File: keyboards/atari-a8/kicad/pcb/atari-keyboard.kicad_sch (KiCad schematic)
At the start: 26 parts, among them J101 PLAYER 1, J102 Conn_02x20_Odd_Even, J103 I2C DISPLAY, J104 Conn_02x20_Odd_Even, J105 Conn_02x20_Odd_Even, J106 Conn_02x20_Odd_Even, SW101 RESET, U101 MAX7219, U102 MAX7219

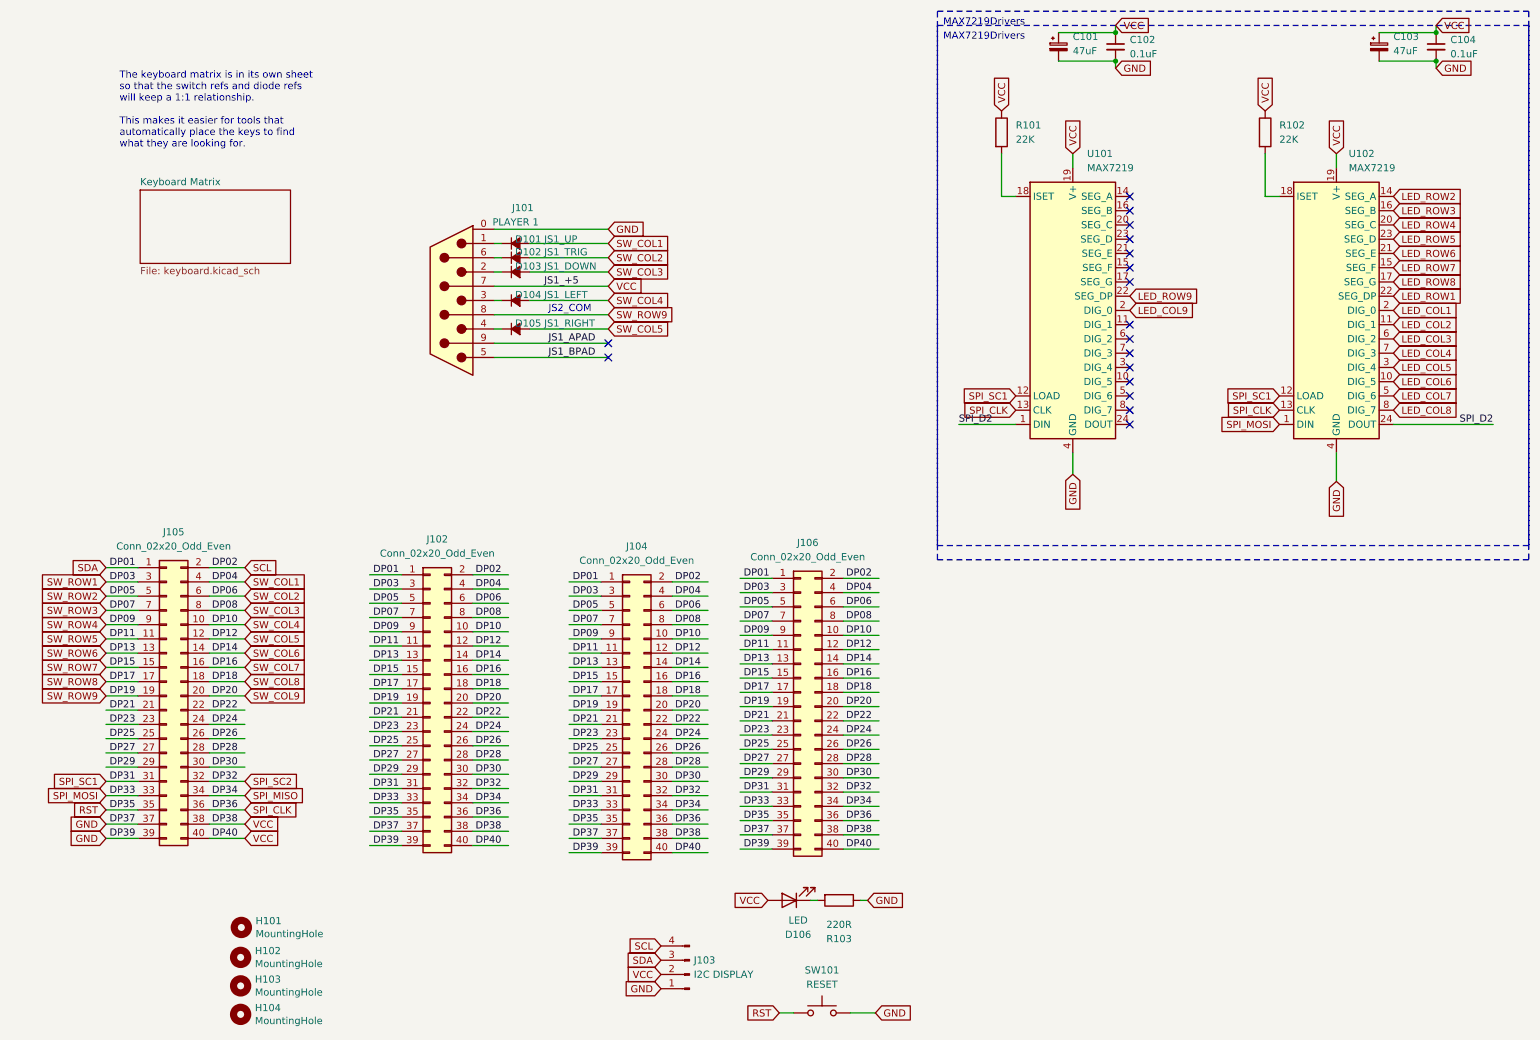
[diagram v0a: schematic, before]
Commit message: Added generating the keyboard plate
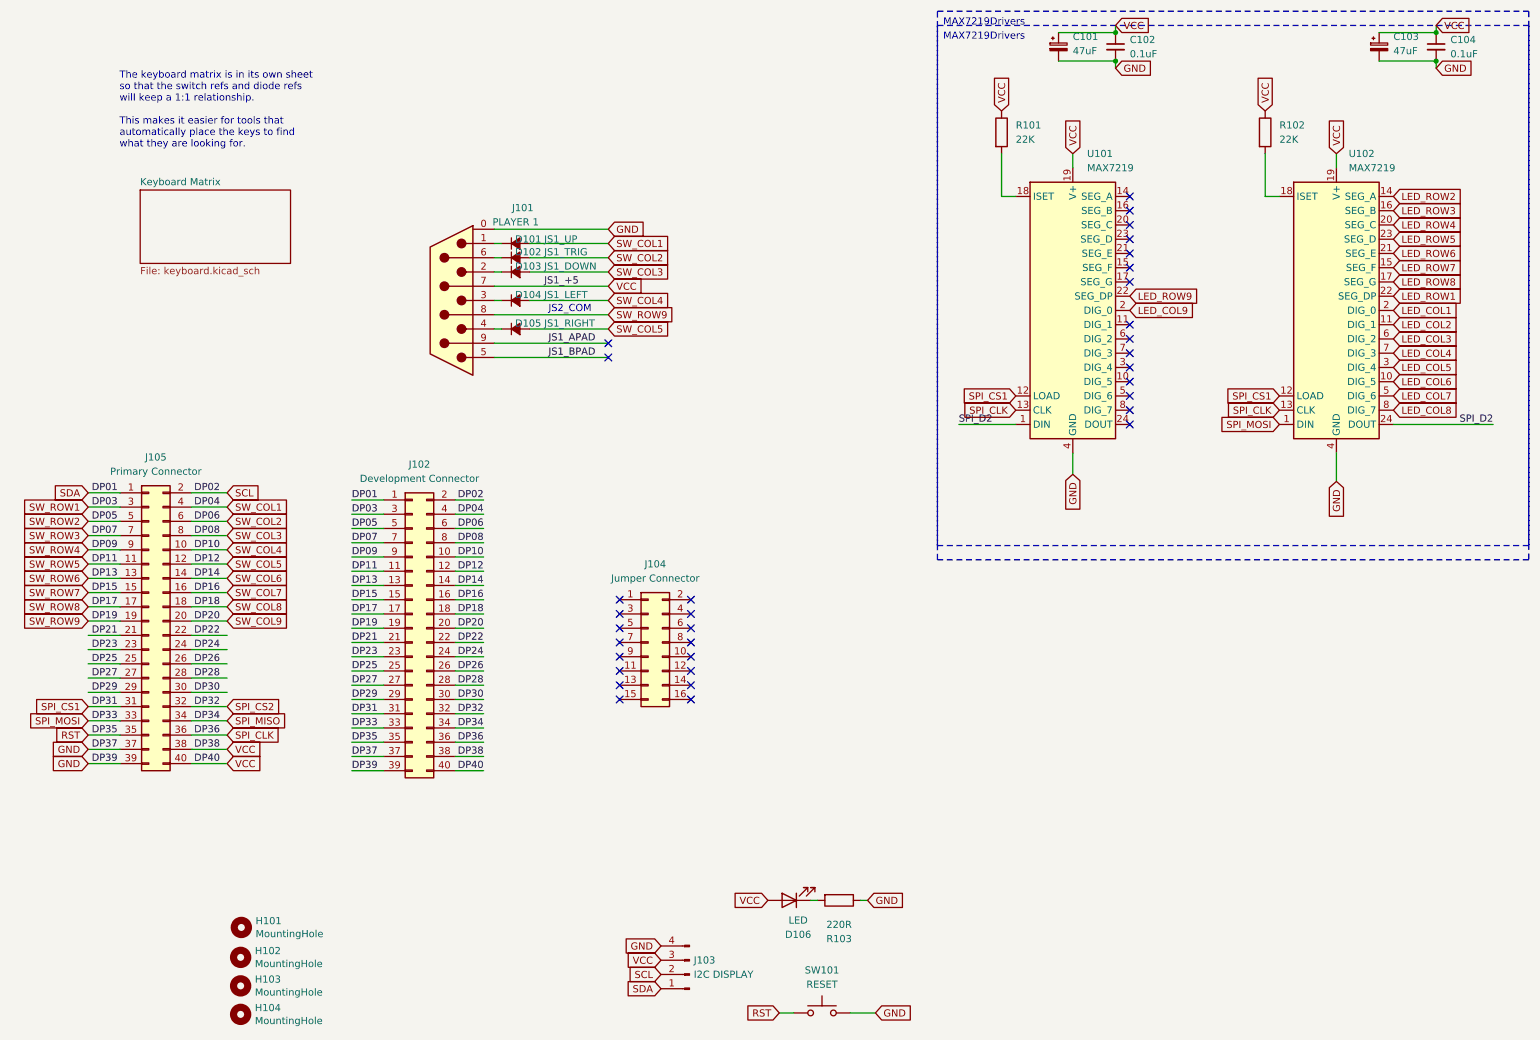
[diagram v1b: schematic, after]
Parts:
- removed J104, J106: Conn_02x20_Odd_Even, Connector_PinSocket_2.54mm:PinSocket_2x20_P2.54mm_Vertical, symbol Connector_Generic:Conn_02x20_Odd_Even
- added J104: Jumper Connector, Connector_PinSocket_2.54mm:PinSocket_2x08_P2.54mm_Vertical, symbol Connector_Generic:Conn_02x08_Odd_Even
- J102: value Conn_02x20_Odd_Even -> Development Connector
- J105: value Conn_02x20_Odd_Even -> Primary Connector
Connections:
- net GND: now also J103.4 (Pin_4); no longer J103.1 (Pin_1)
- net SCL: now also J103.2 (Pin_2); no longer J103.4 (Pin_4)
- net SDA: now also J103.1 (Pin_1); no longer J103.3 (Pin_3)
- net VCC: now also J103.3 (Pin_3); no longer J103.2 (Pin_2)
- net SPI_SC1 renamed SPI_CS1
- net SPI_SC2 renamed SPI_CS2
- no-connect marks 17 -> 33
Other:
- moved on the sheet: J102, J105
